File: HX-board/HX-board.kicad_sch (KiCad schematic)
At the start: 14 parts, among them J1 Testpoints, J2 PCIE-LP-01-01-F-DV-A-TR, J3 DB15_Female, J4 Testpoints, J5 DB15_Female, J6 Testpoints, U1 HX711_Breakout

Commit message: Updated HX, TC boards.
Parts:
- removed U?: CD74HC4067SM, Package_SO:SSOP-24_5.3x8.2mm_P0.65mm, symbol 74xx:CD74HC4067SM
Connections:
- net HX1_CLK is gone; now on net HX_CLK: U1.9 (SCK)
- net HX2_CLK is gone; now on net HX_CLK: U?.9 (SCK)
- net HX3_CLK is gone; now on net HX_CLK: U?.9 (SCK)
- net HX4_CLK is gone; now on net HX_CLK: U?.9 (SCK)
- net HX5_CLK is gone; now on net HX_CLK: U?.9 (SCK)
- net HX6_CLK is gone; now on net HX_CLK: U?.9 (SCK)
- net HX7_CLK is gone; now on net HX_CLK: U?.9 (SCK)
- net +5V: now also J2.A12, J2.A13
- net GND: now also J2.A11, J2.A14, J2.A3, J2.A7, J2.B11, J2.B14, J2.B4, J2.B8
- net HX1_DT: now also J2.A4
- net HX2_DT: now also J2.A5
- net HX3_DT: now also J2.A6
- net HX4_DT: now also J2.B5
- net HX5_DT: now also J2.B6
- net HX6_DT: now also J2.B7
- net HX7_DT: now also J2.A8
- net HX_CLK: now reaches J2.A10
- no-connect marks 26 -> 44
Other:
- note removed: "Double 16-bit multiplexer"

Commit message: Updated schematics of TC,PT
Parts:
- removed U1, U? (x6): HX711_Breakout, Ellie:HX711_Breakout_Board, symbol ELLIE:HX711_Breakout
- added C? (x7): 0.1uF, symbol Device:C_Small
- added C? (x14): 10uF, symbol Device:C_Small
- added Q? (x7): MMBT4403LT3G, Package_TO_SOT_SMD:SOT-23, symbol Transistor_BJT:MMBT3906
- added R? (x7): 20kΩ, symbol Device:R_Small_US
- added R? (x7): 100Ω, symbol Device:R_Small_US
- added R? (x7): 8.2kΩ, symbol Device:R_Small_US
- added U1, U2, U3, U4, U5, U6, U7: HX711, Package_SO:SOP-16_3.9x9.9mm_P1.27mm, symbol Analog_ADC:HX711
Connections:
- net +5V: now also J2.A14, C?.2, C?.2, C?.2, C?.2, C?.2, C?.2, C?.2, Q?.2 (E), Q?.2 (E), Q?.2 (E), Q?.2 (E), Q?.2 (E), Q?.2 (E), Q?.2 (E), U1.1 (VSUP), U1.16 (DVDD), U2.1 (VSUP), U2.16 (DVDD), U3.1 (VSUP), U3.16 (DVDD), U4.1 (VSUP), U4.16 (DVDD), U5.1 (VSUP), U5.16 (DVDD), U6.1 (VSUP), U6.16 (DVDD), U7.1 (VSUP), U7.16 (DVDD); no longer J2.A12
- net GND: now also J1.10 (Pin_10), J1.14 (Pin_14), J1.2 (Pin_2), J1.6 (Pin_6), J2.A12, J2.A15, J2.A6, J2.B12, J2.B15, J2.B3, J3.11 (P111), J3.13 (P13), J3.15 (P15), J3.9 (P9), J4.10 (Pin_10), J4.2 (Pin_2), J4.6 (Pin_6), J5.11 (P111), J5.13 (P13), J5.9 (P9), C?.1, C?.1, C?.1, C?.1, C?.1, C?.1, C?.1, C?.1, C?.1, C?.1, C?.1, C?.1, C?.1, C?.1, C?.1, C?.1, C?.1, C?.1, C?.1, C?.1, C?.1, R?.1, R?.1, R?.1, R?.1, R?.1, R?.1, R?.1, U1.10 (INB+), U1.14 (XI), U1.15 (RATE), U1.5 (AGND), U1.9 (INB-), U2.10 (INB+), U2.14 (XI), U2.15 (RATE), U2.5 (AGND), U2.9 (INB-), U3.10 (INB+), U3.14 (XI), U3.15 (RATE), U3.5 (AGND), U3.9 (INB-), U4.10 (INB+), U4.14 (XI), U4.15 (RATE), U4.5 (AGND), U4.9 (INB-), U5.10 (INB+), U5.14 (XI), U5.15 (RATE), U5.5 (AGND), U5.9 (INB-), U6.10 (INB+), U6.14 (XI), U6.15 (RATE), U6.5 (AGND), U6.9 (INB-), U7.10 (INB+), U7.14 (XI), U7.15 (RATE), U7.5 (AGND), U7.9 (INB-); no longer J2.A11, J2.A14, J2.A7, J2.B11, J2.B14, J2.B4
- net HX1_DT: now also J2.B4, U1.12 (DOUT); no longer J2.A4
- net HX1_E+: now also C?.2, Q?.3 (C), R?.2, U1.3 (AVDD)
- net HX2_DT: now also J2.B5, U2.12 (DOUT); no longer J2.A5
- net HX2_E+: now also C?.2, Q?.3 (C), R?.2, U2.3 (AVDD)
- net HX3_DT: now also J2.B6, U3.12 (DOUT); no longer J2.A6
- net HX3_E+: now also C?.2, Q?.3 (C), R?.2, U3.3 (AVDD)
- net HX4_DT: now also J2.B7, U4.12 (DOUT); no longer J2.B5
- net HX4_E+: now also J1.13 (Pin_13), J3.7, C?.2, Q?.3 (C), R?.2, U4.3 (AVDD); no longer J4.1 (Pin_1), J5.1
- net HX5_DT: now also J2.A7, U5.12 (DOUT); no longer J2.B6
- net HX5_E+: now also J4.1 (Pin_1), J5.1, C?.2, Q?.3 (C), R?.2, U5.3 (AVDD); no longer J4.5 (Pin_5), J5.3
- net HX6_DT: now also J2.A8, U6.12 (DOUT); no longer J2.B7
- net HX6_E+: now also J4.5 (Pin_5), J5.3, C?.2, Q?.3 (C), R?.2, U6.3 (AVDD); no longer J4.9 (Pin_9), J5.5
- net HX7_DT: now also J2.A9, U7.12 (DOUT); no longer J2.A8
- net HX7_E+: now also J4.9 (Pin_9), J5.5, C?.2, Q?.3 (C), R?.2, U7.3 (AVDD); no longer J1.13 (Pin_13), J3.7
- net HX_CLK: now also U1.11 (PD_SCK), U2.11 (PD_SCK), U3.11 (PD_SCK), U4.11 (PD_SCK), U5.11 (PD_SCK), U6.11 (PD_SCK), U7.11 (PD_SCK)
- net HX4_A: now reaches J1.15 (Pin_15)
- net HX4_A: now also J3.8, R?.2
- net HX1_A+ renamed HX1_A
- net HX1_A: now also R?.2
- removed net HX1_A-: J1.2 (Pin_2), J1.4 (Pin_4), J3.10 (P10), J3.9 (P9)
- net HX2_A+ renamed HX2_A
- net HX2_A: now also R?.2
- removed net HX2_A-: J1.6 (Pin_6), J1.8 (Pin_8), J3.11 (P111), J3.12 (P12)
- net HX3_A+ renamed HX3_A
- net HX3_A: now also R?.2
- removed net HX3_A-: J1.10 (Pin_10), J1.12 (Pin_12), J3.13 (P13), J3.14 (P14)
- net HX4_A+ renamed HX5_A
- net HX5_A: now also R?.2
- removed net HX4_A-: J4.2 (Pin_2), J4.4 (Pin_4), J5.10 (P10), J5.9 (P9)
- net HX5_A+ renamed HX6_A
- net HX6_A: now also R?.2
- removed net HX5_A-: J4.6 (Pin_6), J4.8 (Pin_8), J5.11 (P111), J5.12 (P12)
- net HX6_A+ renamed HX7_A
- net HX7_A: now also R?.2
- removed net HX6_A-: J4.10 (Pin_10), J4.12 (Pin_12), J5.13 (P13), J5.14 (P14)
- net HX7_A+: no longer names the net of J4.13 (Pin_13)
- net HX7_A+: no longer J5.7
- removed net HX7_A-: J1.14 (Pin_14), J3.15 (P15), J4.14 (Pin_14), J5.15 (P15)
- new net: Q?.1 (B), U1.2 (BASE)
- new net: R?.1, R?.2, U1.4 (VFB)
- new net: C?.2, U1.6 (VBG)
- new net: R?.1, U1.7 (INA-), U1.8 (INA+)
- new net: C?.2, U5.6 (VBG)
- new net: R?.1, R?.2, U3.4 (VFB)
- new net: R?.1, U2.7 (INA-), U2.8 (INA+)
- new net: R?.1, U4.7 (INA-), U4.8 (INA+)
- new net: R?.1, U6.7 (INA-), U6.8 (INA+)
- new net: R?.1, U7.7 (INA-), U7.8 (INA+)
- new net: Q?.1 (B), U5.2 (BASE)
- new net: Q?.1 (B), U4.2 (BASE)
- new net: R?.1, R?.2, U5.4 (VFB)
- new net: R?.1, U5.7 (INA-), U5.8 (INA+)
- new net: Q?.1 (B), U3.2 (BASE)
- new net: C?.2, U3.6 (VBG)
- new net: R?.1, U3.7 (INA-), U3.8 (INA+)
- new net: Q?.1 (B), U6.2 (BASE)
- new net: R?.1, R?.2, U6.4 (VFB)
- new net: C?.2, U6.6 (VBG)
- new net: C?.2, U4.6 (VBG)
- new net: Q?.1 (B), U7.2 (BASE)
- new net: R?.1, R?.2, U4.4 (VFB)
- new net: Q?.1 (B), U2.2 (BASE)
- new net: R?.1, R?.2, U2.4 (VFB)
- new net: C?.2, U2.6 (VBG)
- new net: R?.1, R?.2, U7.4 (VFB)
- new net: C?.2, U7.6 (VBG)
- no-connect marks 44 -> 51
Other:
- moved on the sheet: J1, J2, J3, J4, J5, J6

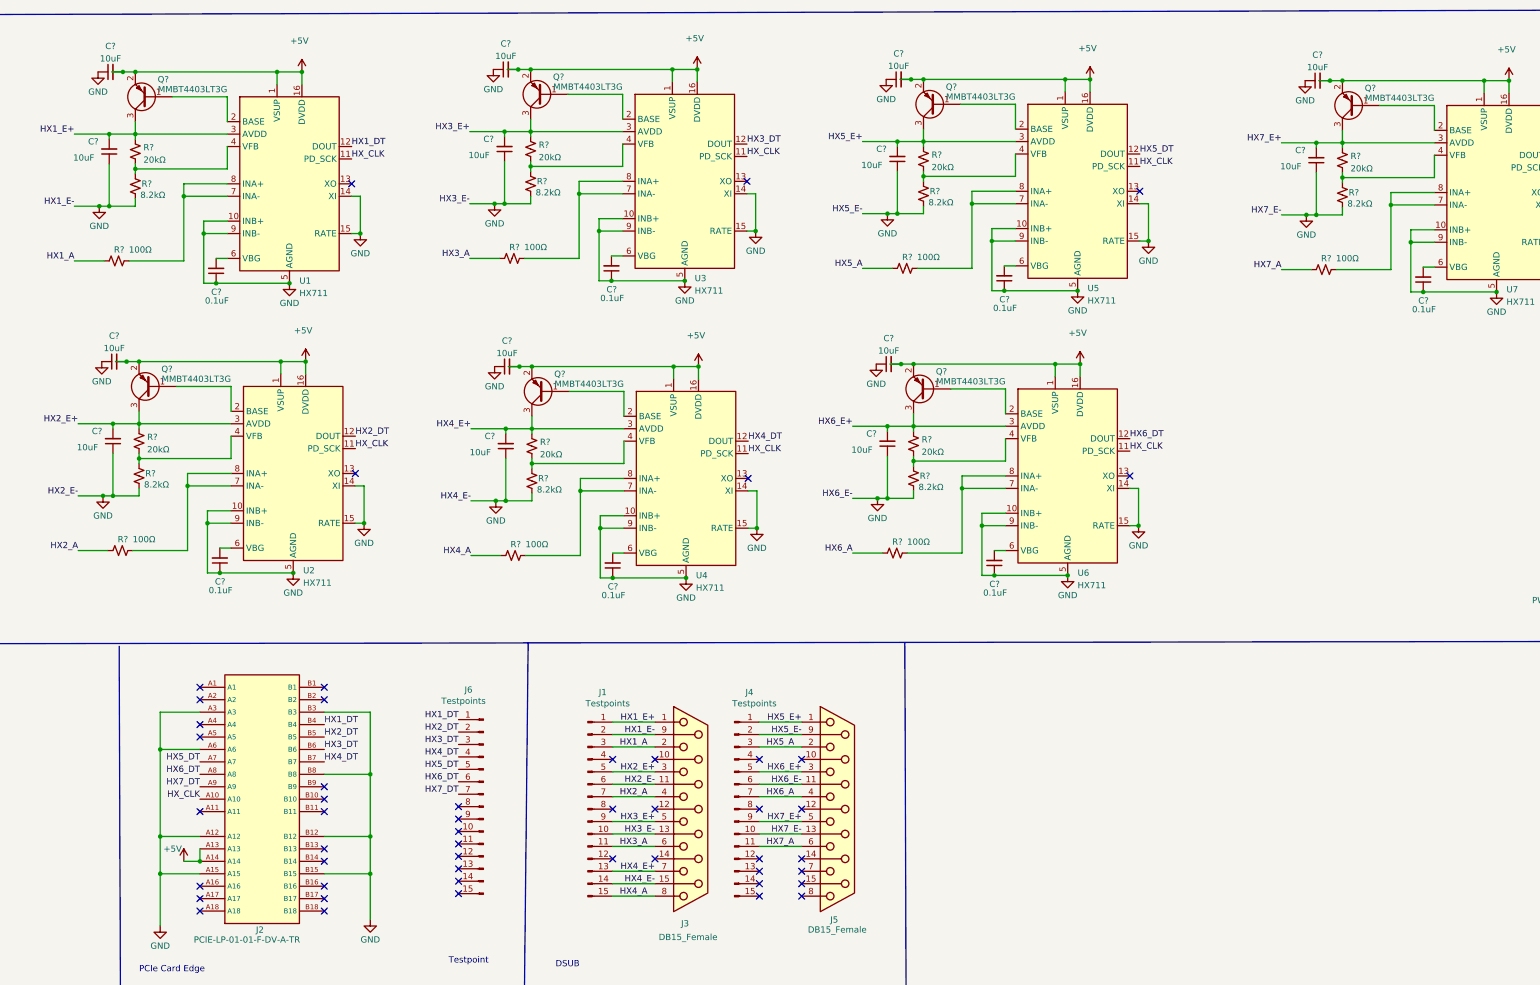
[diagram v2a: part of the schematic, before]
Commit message: Updated HX, TC, and MOSFET board.
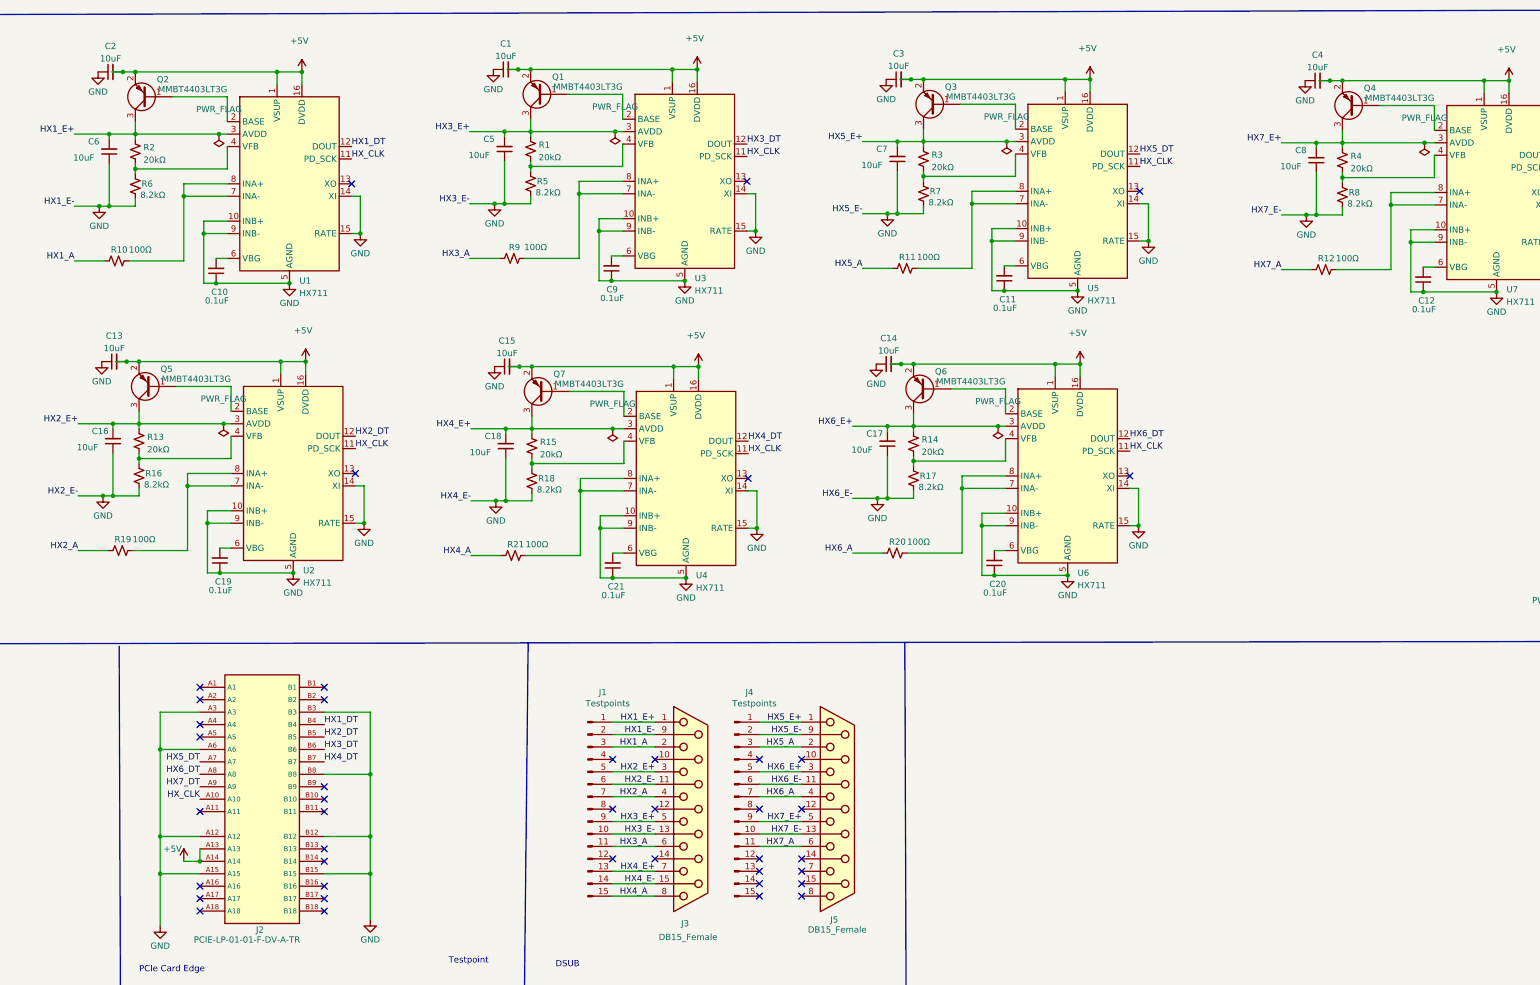
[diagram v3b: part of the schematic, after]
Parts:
- removed J6: Testpoints, Connector_PinHeader_2.54mm:PinHeader_1x15_P2.54mm_Vertical, symbol Connector:Conn_01x15_Male
- C1, C10, C11, C12, C13, C14, C15, C16, C17, C18, C19, C2, C20, C21, C3, C4, C5, C6, C7, C8, C9: renamed from C?; footprint (none) -> Capacitor_SMD:C_0603_1608Metric
- J1, J4: footprint Connector_PinHeader_2.54mm:PinHeader_1x15_P2.54mm_Vertical -> Connector_PinHeader_1.27mm:PinHeader_1x15_P1.27mm_Vertical
- J2: footprint PCIe_x1_card_edge:PCIe_x1_card_edge -> Connector_PCBEdge:BUS_PCIexpress_x1
- R1, R10, R11, R12, R13, R14, R15, R16, R17, R18, R19, R2, R20, R21, R3, R4, R5, R6, R7, R8, R9: renamed from R?; footprint (none) -> Resistor_SMD:R_0603_1608Metric
- gave numbers to parts that had none: 7
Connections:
- no-connect marks 51 -> 43

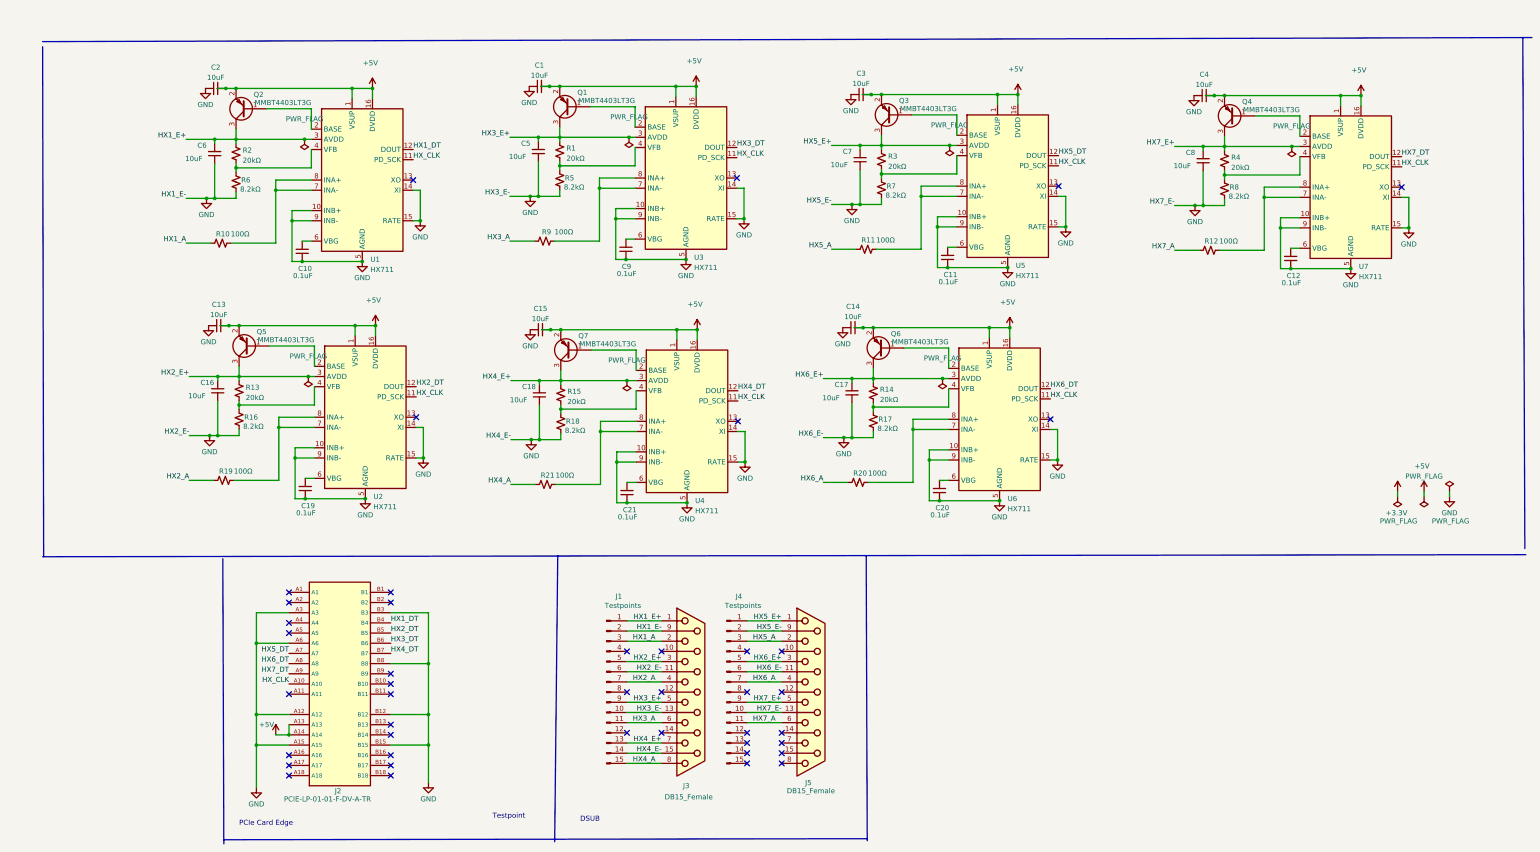
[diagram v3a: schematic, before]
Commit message: Updated pcie and fixed HX, MOSFET, TC board. Also added hierarchical sheet.
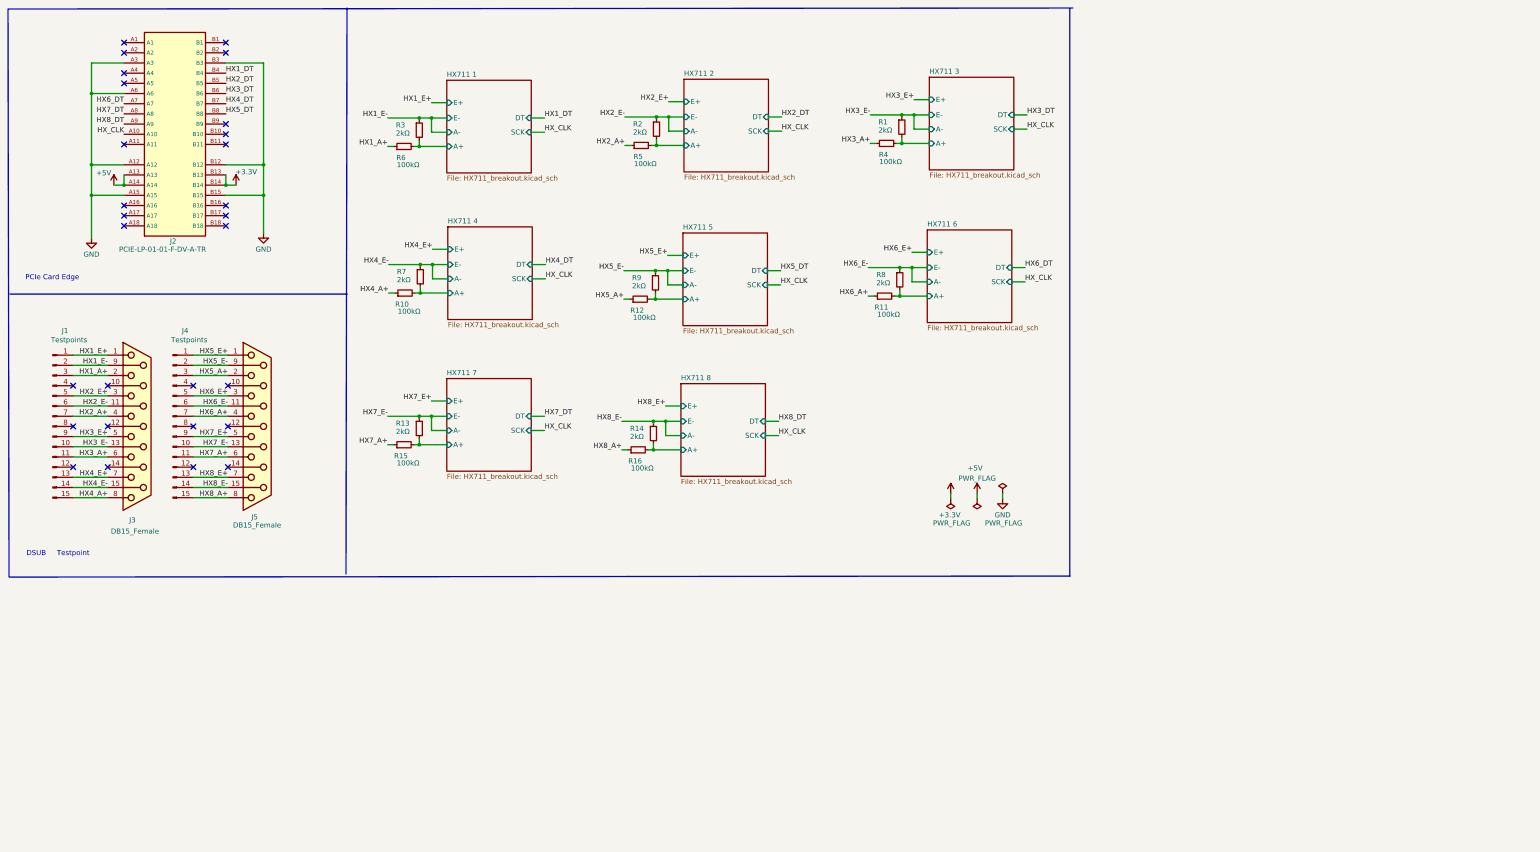
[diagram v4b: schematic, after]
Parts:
- removed C1, C13, C14, C15, C16, C17, C18, C2, C3, C4, C5, C6, C7, C8: 10uF, Capacitor_SMD:C_0603_1608Metric, symbol Device:C_Small
- removed C10, C11, C12, C19, C20, C21, C9: 0.1uF, Capacitor_SMD:C_0603_1608Metric, symbol Device:C_Small
- removed Q1, Q2, Q3, Q4, Q5, Q6, Q7: MMBT4403LT3G, Package_TO_SOT_SMD:SOT-23, symbol Transistor_BJT:MMBT3906
- removed R1, R13, R14, R15, R2, R3, R4: 20kΩ, Resistor_SMD:R_0603_1608Metric, symbol Device:R_Small_US
- removed R10, R11, R12, R19, R20, R21, R9: 100Ω, Resistor_SMD:R_0603_1608Metric, symbol Device:R_Small_US
- removed R16, R17, R18, R5, R6, R7, R8: 8.2kΩ, Resistor_SMD:R_0603_1608Metric, symbol Device:R_Small_US
- removed U1, U2, U3, U4, U5, U6, U7: HX711, Package_SO:SOP-16_3.9x9.9mm_P1.27mm, symbol Analog_ADC:HX711
- added R1, R13, R14, R2, R3, R7, R8, R9: 2kΩ, Resistor_SMD:R_0603_1608Metric, symbol Device:R_Small
- added R10, R11, R12, R15, R16, R4, R5, R6: 100kΩ, Resistor_SMD:R_0603_1608Metric, symbol Device:R_Small
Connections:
- net +3.3V: now also J2.B13, J2.B14
- net GND: no longer J1.10 (Pin_10), J1.14 (Pin_14), J1.2 (Pin_2), J1.6 (Pin_6), J2.B8, J3.11 (P111), J3.13 (P13), J3.15 (P15), J3.9 (P9), J4.10 (Pin_10), J4.2 (Pin_2), J4.6 (Pin_6), J5.11 (P111), J5.13 (P13), J5.9 (P9)
- net HX5_DT: now also J2.B8; no longer J2.A7
- net HX6_DT: now also J2.A7; no longer J2.A8
- net HX7_DT: now also J2.A8; no longer J2.A9
- net HX8_E+: now reaches J4.13 (Pin_13)
- net HX8_E+: now also J5.7
- net HX8_E-: now reaches J4.14 (Pin_14)
- net HX8_E-: now also J5.15 (P15), R14.1
- net HX8_A+: now reaches J4.15 (Pin_15)
- net HX8_A+: now also J5.8, R16.1
- net HX1_A renamed HX1_A+
- net HX1_A+: now also R6.1
- net HX2_A renamed HX2_A+
- net HX2_A+: now also R5.1
- net HX3_A renamed HX3_A+
- net HX3_A+: now also R4.1
- net HX4_A renamed HX4_A+
- net HX4_A+: now also R10.1
- net HX5_A renamed HX5_A+
- net HX5_A+: now also R12.1
- net HX6_A renamed HX6_A+
- net HX6_A+: now also R11.1
- net HX7_A renamed HX7_A+
- net HX7_A+: now also R15.1
- new net HX1_E-: J1.2 (Pin_2), J3.9 (P9), R3.1
- new net HX2_E-: J1.6 (Pin_6), J3.11 (P111), R2.1
- new net HX3_E-: J1.10 (Pin_10), J3.13 (P13), R1.1
- new net HX4_E-: J1.14 (Pin_14), J3.15 (P15), R7.1
- new net HX5_E-: J4.2 (Pin_2), J5.9 (P9), R9.1
- new net HX6_E-: J4.6 (Pin_6), J5.11 (P111), R8.1
- new net HX711 1/A+: R3.2, R6.2
- new net HX711 2/A+: R2.2, R5.2
- new net HX711 3/A+: R1.2, R4.2
- new net HX711 4/A+: R10.2, R7.2
- new net HX711 5/A+: R12.2, R9.2
- new net HX711 6/A+: R11.2, R8.2
- new net HX711 7/A+: R13.2, R15.2
- new net HX711 8/A+: R14.2, R16.2
- new net HX7_E-: J4.10 (Pin_10), J5.13 (P13), R13.1
- new net HX8_DT: J2.A9
- no-connect marks 43 -> 28
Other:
- added sheet HX711 1 (HX711_breakout.kicad_sch)
- added sheet HX711 2 (HX711_breakout.kicad_sch)
- added sheet HX711 3 (HX711_breakout.kicad_sch)
- added sheet HX711 4 (HX711_breakout.kicad_sch)
- added sheet HX711 5 (HX711_breakout.kicad_sch)
- added sheet HX711 6 (HX711_breakout.kicad_sch)
- added sheet HX711 7 (HX711_breakout.kicad_sch)
- added sheet HX711 8 (HX711_breakout.kicad_sch)
- moved on the sheet: J1, J2, J3, J4, J5
